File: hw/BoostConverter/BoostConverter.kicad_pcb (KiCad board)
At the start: 2 copper layers, 50 x 28 mm, 0 parts

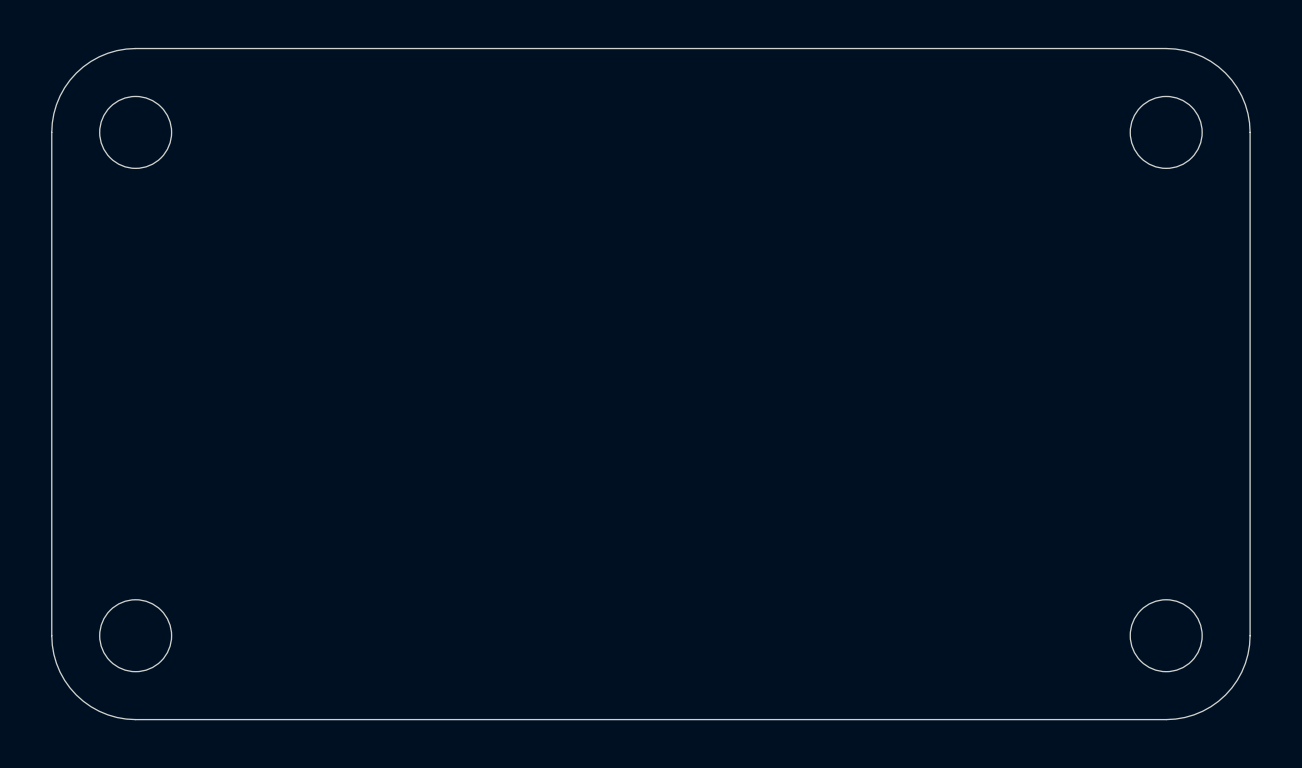
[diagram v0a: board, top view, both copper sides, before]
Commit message: assambled model of the boost dcdc convertor from china
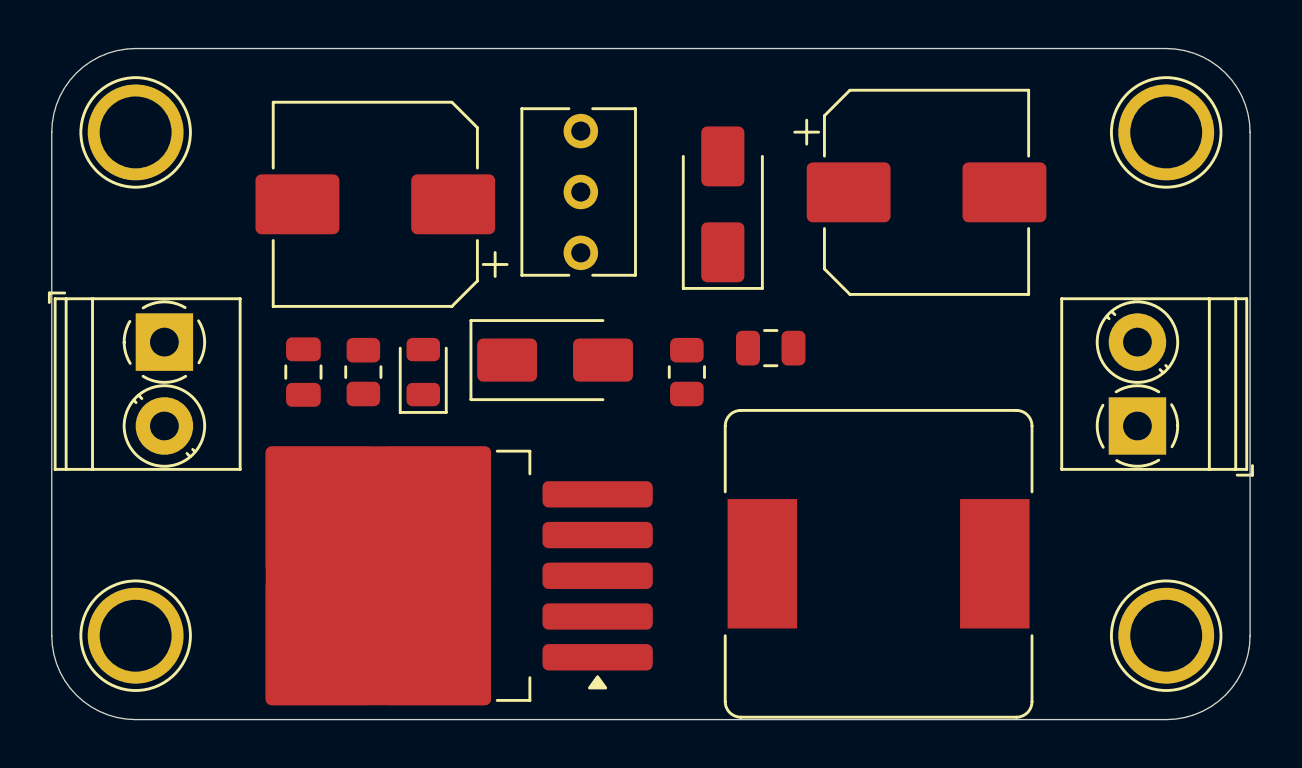
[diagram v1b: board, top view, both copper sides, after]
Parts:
- added C1: C_Polarized, Capacitor_SMD:CP_Elec_8x10, F.Cu at (127.5, 61.5)
- added C2: C_Polarized, Capacitor_SMD:CP_Elec_8x10, F.Cu at (150.5, 61.0)
- added C3: C, Capacitor_SMD:C_0805_2012Metric, F.Cu at (124.5, 68.5)
- added C4: C, Capacitor_SMD:C_0805_2012Metric, F.Cu at (144.0, 67.5)
- added D1: DIODE, Diode_SMD:D_SMA, F.Cu at (142.0, 61.5)
- added D2: DIODE, Diode_SMD:D_SMA, F.Cu at (135.0, 68.0)
- added D3: LED, LED_SMD:LED_0805_2012Metric, F.Cu at (129.5, 68.5)
- added H1: MountingHole_Pad, TestPoint:TestPoint_Plated_Hole_D3.0mm, F.Cu at (160.5, 79.5)
- added H2: MountingHole_Pad, TestPoint:TestPoint_Plated_Hole_D3.0mm, F.Cu at (117.5, 58.5)
- added H3: MountingHole_Pad, TestPoint:TestPoint_Plated_Hole_D3.0mm, F.Cu at (117.5, 79.5)
- added H4: MountingHole_Pad, TestPoint:TestPoint_Plated_Hole_D3.0mm, F.Cu at (160.5, 58.5)
- added J1: Screw_Terminal_01x02, TerminalBlock_Phoenix:TerminalBlock_Phoenix_PT-1,5-2-3.5-H_1x02_P3.50mm_Horizontal, F.Cu at (159.3, 70.8)
- added J2: Screw_Terminal_01x02, TerminalBlock_Phoenix:TerminalBlock_Phoenix_PT-1,5-2-3.5-H_1x02_P3.50mm_Horizontal, F.Cu at (118.7, 67.2)
- added L1: L, Inductor_SMD:L_Bourns_SRR1260, F.Cu at (148.5, 76.5)
- added R1: R, Resistor_SMD:R_0805_2012Metric, F.Cu at (140.5, 68.5)
- added R2: R, Resistor_SMD:R_0805_2012Metric, F.Cu at (127.0, 68.5)
- added RV1: R_Potentiometer, Potentiometer_THT:Potentiometer_Bourns_3266Y_Vertical, F.Cu at (136.1, 63.5)
- added U1: LM2595S-5, Package_TO_SOT_SMD:TO-263-5_TabPin3, F.Cu at (129.1, 77.0)
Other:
- outline, holes or cut-outs redrawn
- copper layers 2 -> 11
